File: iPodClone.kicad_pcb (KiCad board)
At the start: 2 copper layers, 21 parts, among them CN2 PJ-3537S, J1 1769, Q1 MMBT2222ALT1G, U1 V3S, U2 ESP32-D0WD-V3, U3 SGTL5000XNAA3R2, U4 AI12, U5 10104110-0001LF, U6 EA3036C, U7 TSC2046IPWR_C8954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

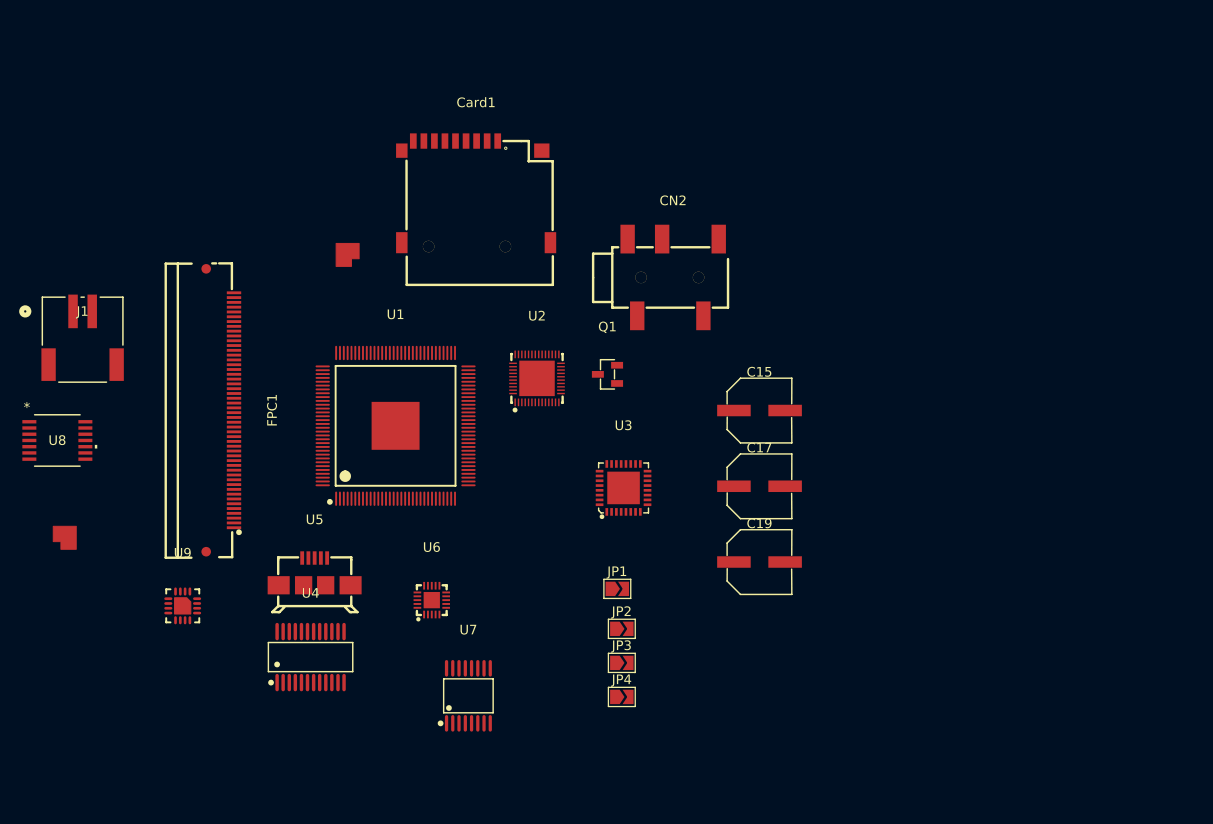
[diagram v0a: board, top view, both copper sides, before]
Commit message: power changes, audio changes, testing layout
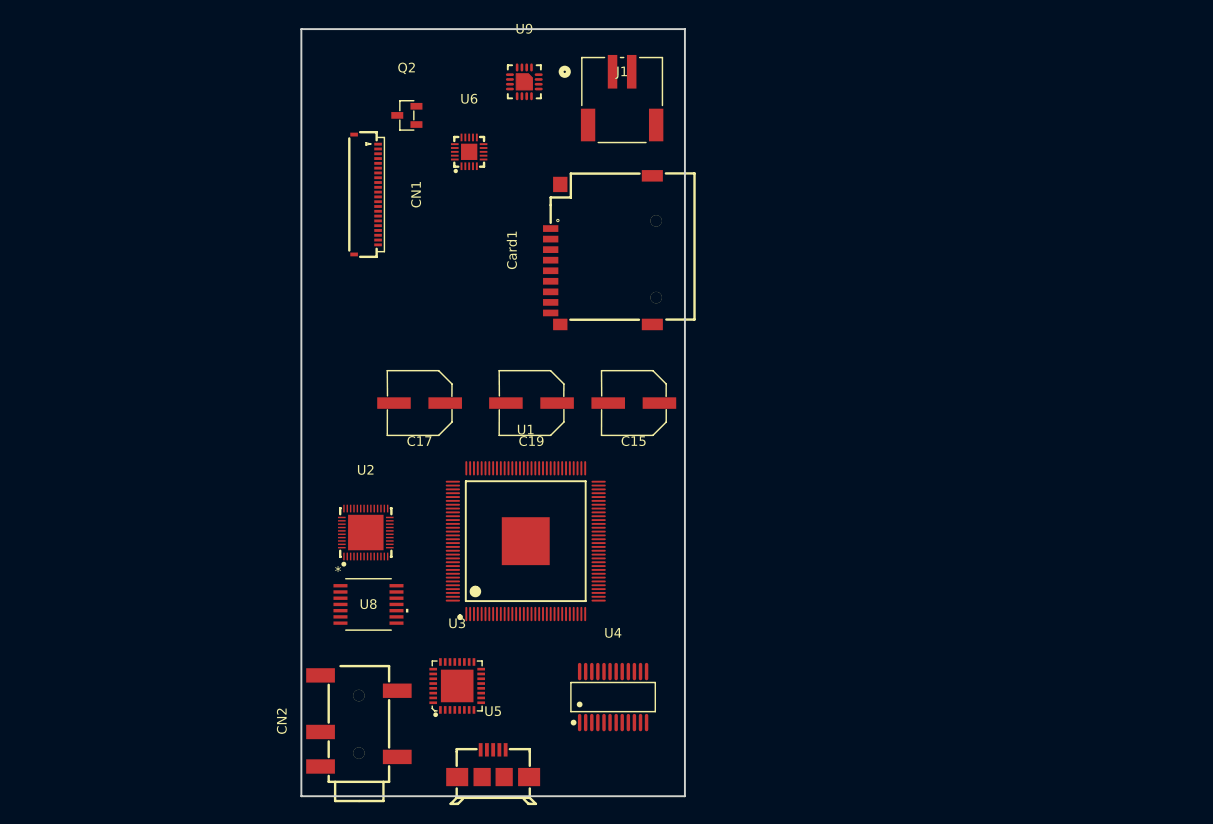
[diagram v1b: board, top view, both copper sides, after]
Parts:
- removed FPC1: 62684-502100ALF, easyeda2kicad:FPC-SMD_50P-P0.50_62684-501100ALF
- removed JP1, JP2, JP3, JP4: SolderJumper_2_Open, Jumper:SolderJumper-2_P1.3mm_Open_TrianglePad1.0x1.5mm
- removed Q1: MMBT2222ALT1G, easyeda2kicad:SOT-23-3_L2.9-W1.3-P1.90-LS2.4-BR
- removed U7: TSC2046IPWR_C8954, easyeda2kicad:TSSOP-16_L5.0-W4.4-P0.65-LS6.4-BL
- added CN1: HC-FPC-05-09-22RLTAG, easyeda2kicad:CONN-SMD_22P-P0.50_HCTL_HC-FPC-05-09-22RLTAG, F.Cu at (136.8, 77.2)
- added Q2: MMBT2222ALT1G, easyeda2kicad:SOT-23-3_L2.9-W1.3-P1.90-LS2.4-BR, F.Cu at (141.0, 69.0)
- moved U9 65.2 mm to (153.2, 65.5)
- moved J1 61.6 mm to (162.4, 64.5)
- moved CN2 56.7 mm to (136.0, 132.2), turned to 90 degrees
- moved U6 46.9 mm to (147.5, 72.8)
- moved U8 36.7 mm to (137.0, 120.0)
- moved C17 36.5 mm to (142.3, 99.0), turned to 180 degrees
- moved U4 31.8 mm to (162.5, 129.7)
- moved C19 29.0 mm to (154.0, 99.0), turned to 180 degrees
- moved U5 27.3 mm to (150.0, 136.6)
- moved U3 27.0 mm to (146.2, 128.5)
- moved U2 24.0 mm to (136.7, 112.5)
- moved U1 18.1 mm to (153.4, 113.4)
- moved Card1 14.4 mm to (161.3, 83.0), turned to 90 degrees
- moved C15 13.1 mm to (164.7, 99.0), turned to 180 degrees
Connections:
- C15 pad 2: VBUS -> +5V
- J1 pad 1: unconnected-(J1-Pad1) -> GND
- J1 pad 2: unconnected-(J1-Pad2) -> +VBAT
- U1 pad 11: LCD_D21 -> unconnected-(U1-PE19/CSI_D15/LCD_D21-Pad11)
- U1 pad 13: LCD_D20 -> unconnected-(U1-PE18/CSI_D14/LCD_D20-Pad13)
- U1 pad 14: LCD_D19 -> unconnected-(U1-PE17/CSI_D13/LCD_D19-Pad14)
- U1 pad 15: LCD_D18 -> unconnected-(U1-PE16/CSI_D12/LCD_D18-Pad15)
- U1 pad 16: LCD_D15 -> unconnected-(U1-PE15/CSI_D11/LCD_D15-Pad16)
- U1 pad 17: LCD_D14 -> unconnected-(U1-PE14/CSI_D10/LCD_D14-Pad17)
- U1 pad 18: LCD_D13 -> unconnected-(U1-PE13/CSI_D9/LCD_D13-Pad18)
- U1 pad 22: LCD_D12 -> unconnected-(U1-PE12/CSI_D8/LCD_D12-Pad22)
- U1 pad 23: LCD_D11 -> unconnected-(U1-PE11/CSI_D7/LCD_D11-Pad23)
- U1 pad 24: LCD_D10 -> unconnected-(U1-PE10/CSI_D6/LCD_D10-Pad24)
- U1 pad 27: LCD_D7 -> unconnected-(U1-PE9/CSI_D5/LCD_D7-Pad27)
- U1 pad 28: LCD_D6 -> unconnected-(U1-PE8/CSI_D4/LCD_D6-Pad28)
- U1 pad 30: LCD_D5 -> unconnected-(U1-PE7/CSI_D3/LCD_D5-Pad30)
- U1 pad 31: LCD_D4 -> unconnected-(U1-PE6/CSI_D2/LCD_D4-Pad31)
- U1 pad 32: LCD_D3 -> unconnected-(U1-PE5/CSI_D1/LCD_D3-Pad32)
- U1 pad 33: LCD_D6 -> unconnected-(U1-PE4/CSI_D0/LCD_D2-Pad33)
- U1 pad 34: LCD_VSYNC -> unconnected-(U1-PE3/CSI_VSYNC/LCD_VSYNC-Pad34)
- U1 pad 35: LCD_HSYNC -> unconnected-(U1-PE2/CSI_HSYNC/LCD_HSYNC-Pad35)
- U1 pad 36: LCD_DE -> unconnected-(U1-PE1/CSI_MCLK/LCD_DE-Pad36)
- U1 pad 37: LCD_CLK -> unconnected-(U1-PE0/CSI_PCLK/LCD_CLK-Pad37)
- U1 pad 41: unconnected-(U1-PB2/UART2_RTS/PB_EINT2-Pad41) -> LCD_RST
- U1 pad 44: unconnected-(U1-PB5/PWM1/PB_EINT5-Pad44) -> LCD_DC
- U1 pad 52: TS_MISO -> unconnected-(U1-PC0/SDC2_CLK/SPI_MISO-Pad52)
- U1 pad 53: TS_CLK -> LCD_CLK
- U1 pad 54: TS_CS -> LCD_CS
- U1 pad 55: TS_MOSI -> LCD_MOSI
- U1 pad 6: LCD_D23 -> unconnected-(U1-PE24/LCD_D23-Pad6)
- U1 pad 7: LCD_D22 -> unconnected-(U1-PE23/LCD_D22-Pad7)
- U6 pad 10: VBUS -> +5V
- U6 pad 16: VBUS -> +5V
- U6 pad 18: VBUS -> +5V
- U6 pad 19: VBUS -> +5V
- U6 pad 7: VBUS -> +5V
- U6 pad 8: VBUS -> +5V
- U6 pad 9: VBUS -> +5V
- U8 pad 3: VBUS -> +5V
- U9 pad 1: unconnected-(U9-TS-Pad1) -> Net-(U9-TS)
- U9 pad 10: unconnected-(U9-OUT-Pad10) -> VSYS
- U9 pad 11: unconnected-(U9-OUT-Pad11) -> VSYS
- U9 pad 13: unconnected-(U9-IN-Pad13) -> VBUS
- U9 pad 14: unconnected-(U9-TMR-Pad14) -> GND
- U9 pad 17: unconnected-(U9-EP-Pad17) -> GND
- U9 pad 2: unconnected-(U9-BAT-Pad2) -> +VBAT
- U9 pad 3: unconnected-(U9-BAT-Pad3) -> +VBAT
- U9 pad 4: unconnected-(U9-~{CE}-Pad4) -> GND
- U9 pad 5: unconnected-(U9-EN2-Pad5) -> VSYS
- U9 pad 6: unconnected-(U9-EN1-Pad6) -> GND
- U9 pad 7: unconnected-(U9-~{PGOOD}-Pad7) -> Net-(D2-K)
- U9 pad 8: unconnected-(U9-VSS-Pad8) -> GND
- U9 pad 9: unconnected-(U9-~{CHG}-Pad9) -> Net-(D1-K)
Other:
- board outline added: 40 x 80 mm

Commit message: audio changes, better layout
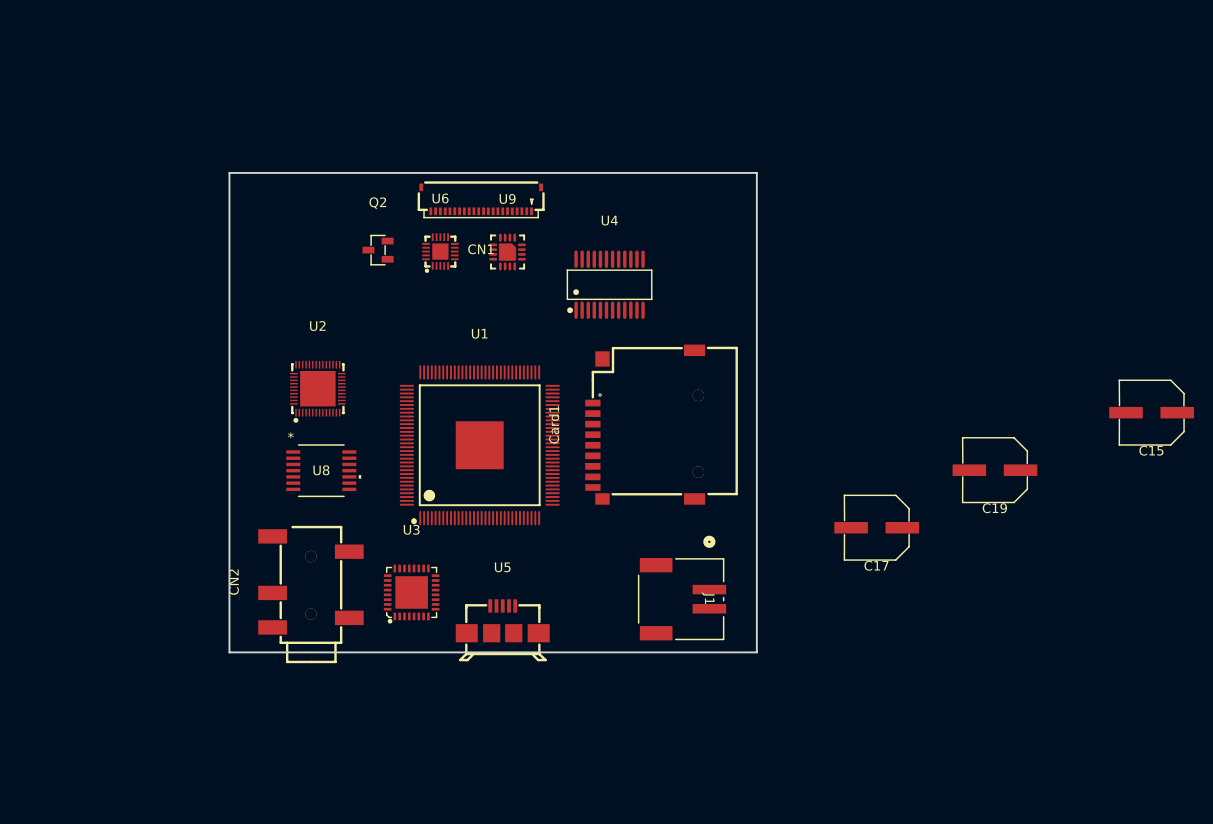
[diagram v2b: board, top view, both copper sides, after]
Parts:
- moved J1 54.9 mm to (172.5, 118.4), turned to -90 degrees
- moved C15 54.0 mm to (218.7, 100.0)
- moved C17 49.4 mm to (190.0, 112.0)
- moved C19 48.8 mm to (202.3, 106.0)
- moved U4 43.0 mm to (162.1, 86.7)
- moved Card1 18.7 mm to (165.7, 101.2)
- moved U9 17.8 mm to (151.5, 83.2)
- moved U2 15.8 mm to (131.7, 97.5)
- moved CN2 15.3 mm to (131.0, 117.7)
- moved U5 15.0 mm to (151.0, 121.6)
- moved U8 14.8 mm to (132.1, 106.0)
- moved Q2 14.4 mm to (138.0, 83.0)
- moved CN1 12.0 mm to (148.8, 77.8), turned to 180 degrees
- moved U1 11.1 mm to (148.6, 103.4)
- moved U3 10.8 mm to (141.5, 118.8)
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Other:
- board size 40 x 80 mm -> 55 x 50 mm

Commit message: before switching to ESP32 module
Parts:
- added X2: XTM32040000JT00351005, easyeda2kicad:CRYSTAL-SMD_4P-L3.2-W2.5-BL, F.Cu at (115.3, 112.5)
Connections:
- CN1 pad 17: LCD_CLK -> SPI_CLK
- CN1 pad 21: LCD_MOSI -> SPI_MOSI
- Card1 pad 4: unconnected-(Card1-VDD-Pad4) -> +3.3V
- U1 pad 37: unconnected-(U1-PE0/CSI_PCLK/LCD_CLK-Pad37) -> PCM_CS
- U1 pad 53: LCD_CLK -> SPI_CLK
- U1 pad 55: LCD_MOSI -> SPI_MOSI
- U2 pad 1: unconnected-(U2-VDDA-Pad1) -> +3.3V
- U2 pad 19: unconnected-(U2-VDD3P3_RTC-Pad19) -> +3.3V
- U2 pad 3: unconnected-(U2-VDD3P3-Pad3) -> Net-(L5-Pad2)
- U2 pad 37: unconnected-(U2-VDD3P3_CPU-Pad37) -> +3.3V
- U2 pad 4: unconnected-(U2-VDD3P3-Pad4) -> Net-(L5-Pad2)
- U2 pad 43: unconnected-(U2-VDDA-Pad43) -> +3.3V
- U2 pad 44: unconnected-(U2-XTAL_N-Pad44) -> /WiFi+BT/XTAL_N
- U2 pad 45: unconnected-(U2-XTAL_P-Pad45) -> /WiFi+BT/XTAL_P
- U2 pad 46: unconnected-(U2-VDDA-Pad46) -> +3.3V
- U2 pad 49: unconnected-(U2-GND-Pad49) -> GND
- U3 pad 13: unconnected-(U3-LINEIN_R-Pad13) -> Net-(U3-LINEIN_R)
- U3 pad 14: unconnected-(U3-LINEIN_L-Pad14) -> Net-(U3-LINEIN_L)
- U3 pad 15: unconnected-(U3-MIC-Pad15) -> Net-(U3-MIC)
- U3 pad 21: unconnected-(U3-SYS_MCLK-Pad21) -> I2S_MCLK
- U5 pad 4: unconnected-(U5-ID-Pad4) -> Net-(U5-ID)
- U8 pad 10: unconnected-(U8-MD-Pad10) -> SPI_MOSI
- U8 pad 11: unconnected-(U8-MC-Pad11) -> SPI_CLK
- U8 pad 12: unconnected-(U8-MS-Pad12) -> PCM_CS
- U8 pad 6: unconnected-(U8-SCKI-Pad6) -> I2S_MCLK
- U9 pad 12: unconnected-(U9-ILIM-Pad12) -> Net-(U9-ILIM)
- U9 pad 16: unconnected-(U9-ISET-Pad16) -> Net-(U9-ISET)

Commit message: gitignore and audio changes
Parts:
- removed C15, C17, C19: GVS1H100M0604, easyeda2kicad:CAP-SMD_BD6.3-L6.6-W6.6-LS7.3
- removed CN2: PJ-3537S, easyeda2kicad:AUDIO-SMD_PJ-3537S
- added CN3: PJ-342, easyeda2kicad:AUDIO-SMD_PJ-342, F.Cu at (128.0, 116.0)
- added U10: F35SQA512M-WWT, easyeda2kicad:WSON-8_L8.0-W6.0-P1.27-BL-EP-1, F.Cu at (161.1, 85.2)
- added U11: XC6206P302MR_C5148691, easyeda2kicad:SOT-23-3_L3.0-W1.7-P0.95-LS2.9-BR, F.Cu at (118.1, 92.4)
- added U7: MT3608, easyeda2kicad:SOT-23-6_L2.9-W1.6-P0.95-LS2.8-BL, F.Cu at (154.1, 90.2)
- added X1: FC-12M32.768KHZ7PF20PPM, easyeda2kicad:FC-12M_L2.0-W1.2, F.Cu at (118.1, 98.0)
- U2: value ESP32-D0WD-V3 -> ESP32-MINI-1-H4; footprint easyeda2kicad:QFN-48_L5.0-W5.0-P0.35-BL-EP3.7 -> easyeda2kicad:WIFI-SMD_ESP32-MINI-1
- U4: value AI12 -> BQ27220YZFR; footprint easyeda2kicad:SSOP-24_L8.8-W4.0-P0.64-LS6.2-BL -> easyeda2kicad:DSBGA-9_L1.7-W1.6-R3-C3-P0.50-BL
- X2: value XTM32040000JT00351005 -> X322524MOB4SI
- moved U4 26.7 mm to (169.7, 112.3)
- moved U2 9.64 mm to (129.8, 88.0)
- moved Q2 2.15 mm to (139.0, 85.0)
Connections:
- net /SDC0_CLK renamed SDC0_CLK
- net /SDC0_CMD renamed SDC0_CMD
- net /SDC0_D0 renamed SDC0_D0
- net /SDC0_D1 renamed SDC0_D1
- net /SDC0_D2 renamed SDC0_D2
- net /SDC0_D3 renamed SDC0_D3
- U1 pad 104: unconnected-(U1-VCC-IO0-Pad104) -> +3.3V
- U1 pad 115: unconnected-(U1-AVCC-Pad115) -> +3V0
- U1 pad 116: unconnected-(U1-AGND-Pad116) -> GND
- U1 pad 117: unconnected-(U1-VRA1-Pad117) -> Net-(U1-VRA1)
- U1 pad 118: unconnected-(U1-VRA2-Pad118) -> Net-(U1-VRA2)
- U1 pad 12: unconnected-(U1-VCC-PE0-Pad12) -> +3.3V
- U1 pad 122: unconnected-(U1-HPVCCIN-Pad122) -> +3.3V
- U1 pad 127: unconnected-(U1-VCC-IO1-Pad127) -> +3.3V
- U1 pad 29: unconnected-(U1-VCC-PE1-Pad29) -> +3.3V
- U1 pad 35: unconnected-(U1-PE2/CSI_HSYNC/LCD_HSYNC-Pad35) -> GPOUT
- U1 pad 36: unconnected-(U1-PE1/CSI_MCLK/LCD_DE-Pad36) -> LCD_CS
- U1 pad 45: SGTL_SCK -> I2C_SCK
- U1 pad 46: SGTL_SDA -> I2C_SDA
- U1 pad 48: unconnected-(U1-PB8/TWI1_SCK/UART0_TX/PB_EINT8-Pad48) -> UART0_TX
- U1 pad 49: unconnected-(U1-PB9/TWI1_SDA/UART0_RX/PB_EINT9-Pad49) -> UART0_RX
- U1 pad 50: unconnected-(U1-VCC-IO3-Pad50) -> +3.3V
- U1 pad 52: unconnected-(U1-PC0/SDC2_CLK/SPI_MISO-Pad52) -> SPI_MISO
- U1 pad 54: LCD_CS -> NAND_CS
- U1 pad 57: unconnected-(U1-VCC-IO2-Pad57) -> +3.3V
- U1 pad 63: unconnected-(U1-SVREF1-Pad63) -> /SVREF
- U1 pad 71: unconnected-(U1-SVREF0-Pad71) -> /SVREF
- U1 pad 73: unconnected-(U1-SZQ-Pad73) -> Net-(U1-SZQ)
- U1 pad 74: unconnected-(U1-X24MOUT-Pad74) -> /X24MOUT
- U1 pad 75: unconnected-(U1-X24MIN-Pad75) -> /X24MIN
- U1 pad 76: unconnected-(U1-VCC-PLL-Pad76) -> +3V0
- U1 pad 8: unconnected-(U1-PE22/CSI_SDA/TWI1_SDA/UART1_RX-Pad8) -> /V3S-ESP32_RX
- U1 pad 88: unconnected-(U1-EPHY-VDD-Pad88) -> +1V2
- U1 pad 9: unconnected-(U1-PE21/CSI_SCK/TWI1_SCK/UART1_TX-Pad9) -> /V3S-ESP32_TX
- U1 pad 95: unconnected-(U1-X32KOUT-Pad95) -> /X32KOUT
- U1 pad 96: unconnected-(U1-X32KIN-Pad96) -> /X32KIN
- U1 pad 97: unconnected-(U1-RTC-VIO-Pad97) -> Net-(U1-RTC-VIO)
- U1 pad 99: unconnected-(U1-RESET-Pad99) -> /RESET
- U2 pad 1: +3.3V -> GND
- U2 pad 19: +3.3V -> unconnected-(U2-IO15-Pad19)
- U2 pad 2: unconnected-(U2-LNA_IN-Pad2) -> GND
- U2 pad 21: unconnected-(U2-MTDO-Pad21) -> I2S_MCLK
- U2 pad 25: unconnected-(U2-GPIO16-Pad25) -> /WiFi+BT/V3S-ESP32_TX
- U2 pad 26: unconnected-(U2-VDD_SDIO-Pad26) -> /WiFi+BT/V3S-ESP32_RX
- U2 pad 27: unconnected-(U2-GPIO17-Pad27) -> GND
- U2 pad 29: unconnected-(U2-SD_DATA_3-Pad29) -> I2S_PCMOUT
- U2 pad 3: Net-(L5-Pad2) -> +3.3V
- U2 pad 30: unconnected-(U2-SD_CMD-Pad30) -> I2S_SCK
- U2 pad 31: unconnected-(U2-SD_CLK-Pad31) -> I2S_WS
- U2 pad 35: unconnected-(U2-GPIO18-Pad35) -> /WiFi+BT/RXD0
- U2 pad 36: unconnected-(U2-GPIO23-Pad36) -> /WiFi+BT/TXD0
- U2 pad 37: +3.3V -> unconnected-(U2-NC-Pad37)
- U2 pad 38: unconnected-(U2-GPIO19-Pad38) -> GND
- U2 pad 39: unconnected-(U2-GPIO22-Pad39) -> GND
- U2 pad 4: Net-(L5-Pad2) -> unconnected-(U2-I36-Pad4)
- U2 pad 40: unconnected-(U2-U0RXD-Pad40) -> GND
- U2 pad 41: unconnected-(U2-U0TXD-Pad41) -> GND
- U2 pad 42: unconnected-(U2-GPIO21-Pad42) -> GND
- U2 pad 43: +3.3V -> GND
- U2 pad 44: /WiFi+BT/XTAL_N -> GND
- U2 pad 45: /WiFi+BT/XTAL_P -> GND
- U2 pad 46: +3.3V -> GND
- U2 pad 47: unconnected-(U2-CAP2-Pad47) -> GND
- U2 pad 48: unconnected-(U2-CAP1-Pad48) -> GND
- U2 pad 8: unconnected-(U2-SENSOR_VN-Pad8) -> /WiFi+BT/EN
- U3 pad 26: I2S_SD -> I2S_PCMOUT
- U3 pad 27: SGTL_SDA -> I2C_SDA
- U3 pad 29: SGTL_SCK -> I2C_SCK
- U8 pad 9: I2S_SD -> I2S_PCMOUT
- X2 pad 1: /WiFi+BT/XTAL_P -> /X24MIN
- X2 pad 3: /WiFi+BT/XTAL_N -> /X24MOUT
